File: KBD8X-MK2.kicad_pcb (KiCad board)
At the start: 2 copper layers, 343.7 x 118.3 mm, 347 parts, among them J1 AVR-ISP-6, Q1 DSS60601MZ4-13, SW1 SW_Push, SW2 SW_SPDT, SW3 SW_SPDT, U1 ATmega32U4-MU, U2 PRTR5V0U2X, Y1 16MHz

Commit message: Added 3U and 10U footprints to the PCB
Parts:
- removed H1: KBD8X-MKII Logo, KBD8X_MK2_Graphics:kbd8x-logo
- removed H2: ai03 logo, KBD8X_MK2_Graphics:ai-ring-6mm-FancyAss
- removed H3: ai03 logo, KBD8X_MK2_Graphics:ai-ring-6mm-FancyAss-Mask
- removed H4: ai03 logo, KBD8X_MK2_Graphics:ai-ring-6mm
- added D15: SOD-123, KBD8X_MK2_Components:D_SOD-123, B.Cu at (219.9, 254.0)
- added D16: SOD-123, KBD8X_MK2_Components:D_SOD-123, B.Cu at (294.0, 254.0)
- added MX_SP3: MX-LED, KBD8X_MK2_Switches:MXOnly-10U-ReversedStabilizers, F.Cu at (267.5, 254.8)
- added MX_SP4: MX-LED, KBD8X_MK2_Switches:MXOnly-1U, F.Cu at (267.5, 254.8)
- added MX_SSPC1: MX-LED, KBD8X_MK2_Switches:MXOnly-3U-ReversedStabilizers, F.Cu at (229.4, 254.8)
- added MX_SSPC2: MX-LED, KBD8X_MK2_Switches:MXOnly-3U-ReversedStabilizers, F.Cu at (305.6, 254.8)
- added R15: 1k, KBD8X_MK2_Components:R_0603, B.Cu at (237.6, 259.4)
- added R34: 1k, KBD8X_MK2_Components:R_0603, B.Cu at (314.4, 259.5)
- RGB1, RGB10, RGB11, RGB12, RGB13, RGB14, RGB15, RGB16, RGB17, RGB18, RGB2, RGB3, RGB4, RGB5, RGB6, RGB7, RGB8, RGB9: footprint LED_SMD:LED_WS2812B_PLCC4_5.0x5.0mm_P3.2mm -> KBD8X_MK2_Components:LED_WS2812B-PLCC4
- U1: footprint Package_DFN_QFN:QFN-44-1EP_7x7mm_P0.5mm_EP5.2x5.2mm -> KBD8X_MK2_Components:QFN-44-1EP_7x7mm_Pitch0.5mm
- moved R87 3.79 mm to (243.9, 259.4)
- moved RGB12 3.29 mm to (239.9, 252.6)
- moved R90 2.35 mm to (337.4, 259.6)
- moved CRGB12 2.35 mm to (243.7, 252.4)
- moved CRGB14 1.93 mm to (312.9, 250.5)
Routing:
- net +5V: track 2658.4 -> 2717.1 mm
- net COL2: track 665.0 -> 686.5 mm
- net COL4: track 605.9 -> 627.4 mm
- net Net-(D16-Pad2): track 0.00 -> 15.7 mm
- net Net-(D15-Pad2): track 0.00 -> 13.1 mm
- net GND: track 1191.1 -> 1200.9 mm
- net Net-(MX_SSPC2-Pad4): track 0.00 -> 8.67 mm
- net Net-(MX_SSPC1-Pad4): track 0.00 -> 7.98 mm
- net ROW11: track 320.9 -> 326.4 mm
- net Net-(MX_SP1-Pad4): track 23.4 -> 28.5 mm
- net Net-(RGB11-Pad2): track 42.6 -> 46.9 mm
- net Net-(MX_RALT1-Pad4): track 6.91 -> 11.0 mm
- net Net-(RGB12-Pad2): track 42.9 -> 39.5 mm
- net ROW10: track 306.0 -> 308.9 mm
- net LEDGND: track 1914.1 -> 1914.9 mm
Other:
- board text removed: "KBD8X-MKII PCB Rev 2.0 20190404"
- board text removed: "kb.ai03.me"

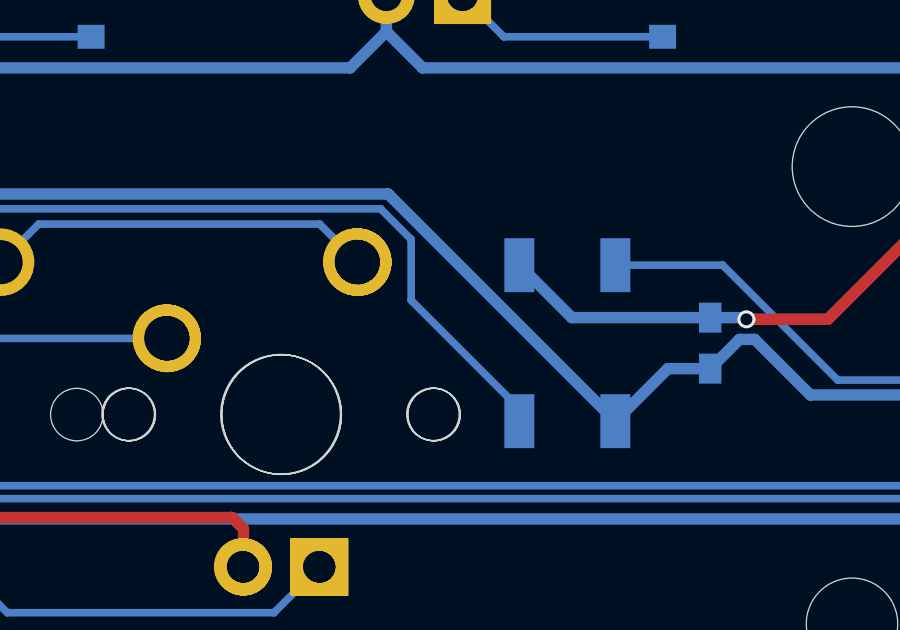
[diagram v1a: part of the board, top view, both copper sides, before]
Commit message: Removed the solder joints on the front layer for the switches
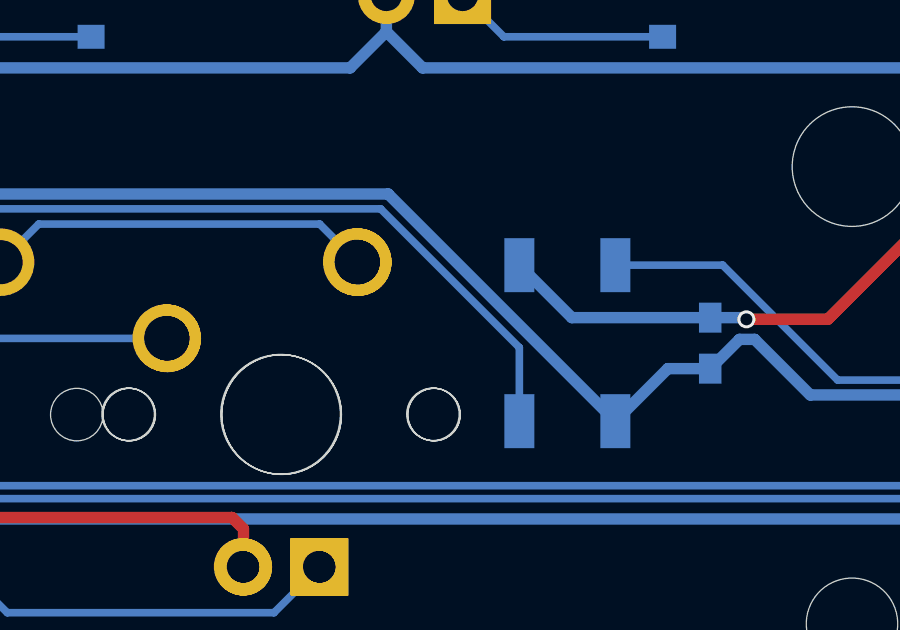
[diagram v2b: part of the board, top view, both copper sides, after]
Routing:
- net +5V: track 2717.1 -> 2725.7 mm
- net Net-(MX_SSPC2-Pad4): track 8.67 -> 0.00 mm
